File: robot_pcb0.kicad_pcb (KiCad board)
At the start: 2 copper layers, 61.9 x 57.8 mm, 73 parts, among them J1 USB_B_Mini, J10 GPIO, J2 CAN, J3 PWR, J4 Power_terminal, J5 Motor1, J6 Motor2, J7 Motor3, J8 Motor4, J9 UART, P1 SWD, U1 TJA1051TK-3, U2 STM32F40X_LQFP64, U3 BMI160, U4 MCP16311/2, U5 MCP16311/2, U6 DRV8833PW, U7 DRV8833PW, Y1 8M

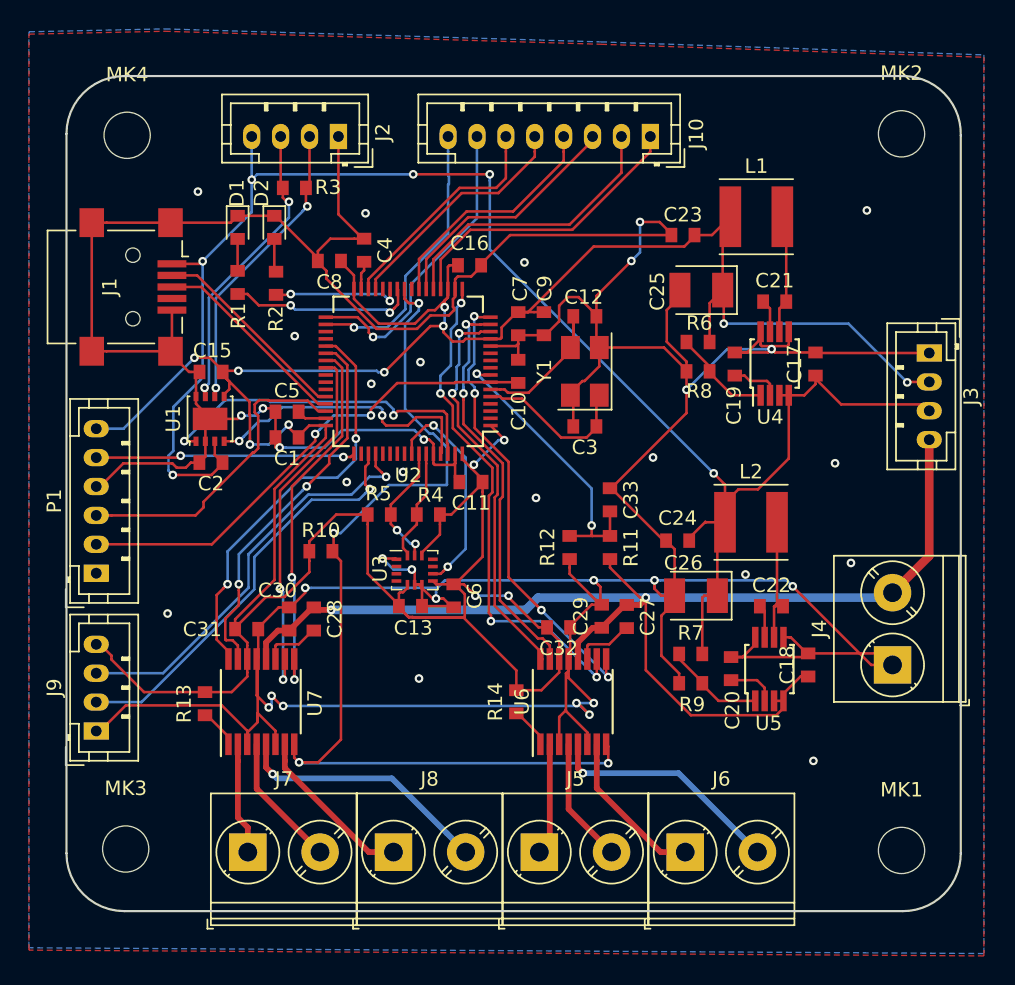
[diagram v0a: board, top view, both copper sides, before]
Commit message: adding an nrf52
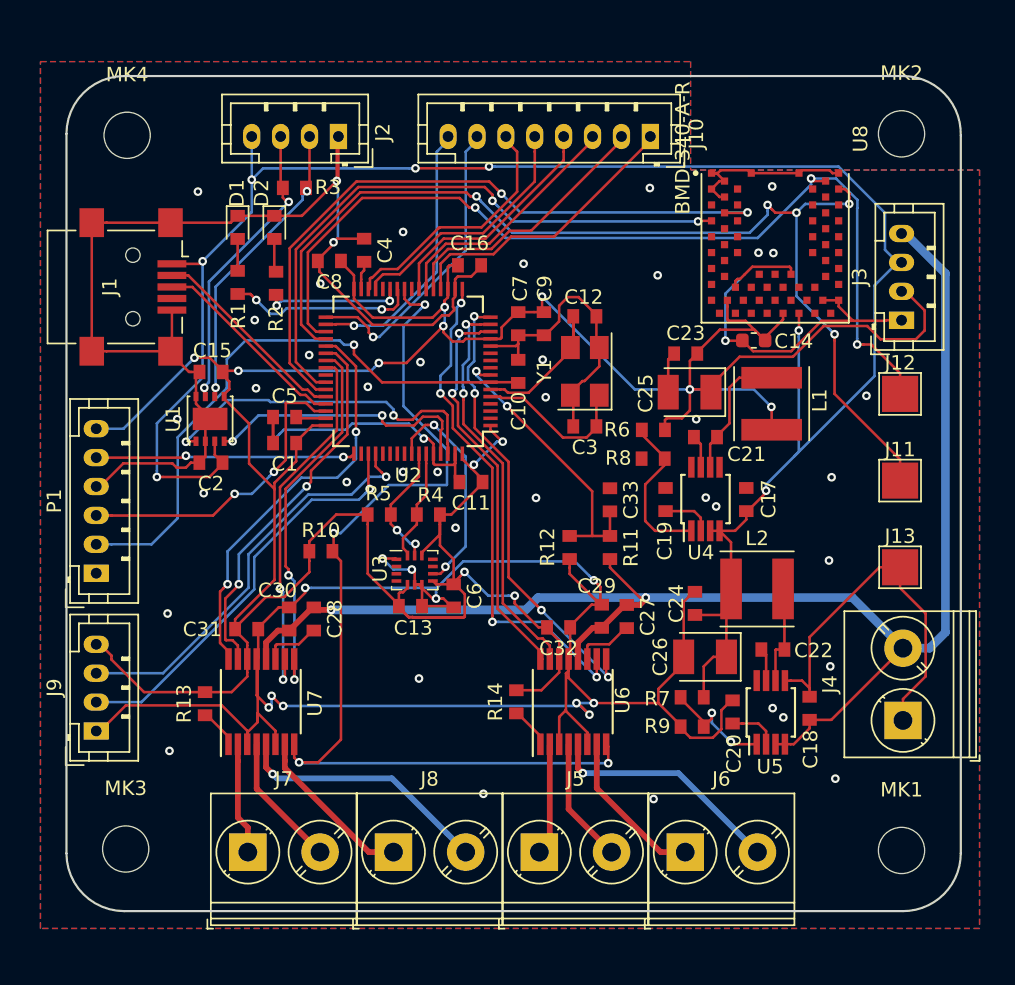
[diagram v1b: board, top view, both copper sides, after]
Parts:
- added C14: 2.2u, Capacitor_SMD:C_0603_1608Metric, F.Cu at (131.9, 89.3)
- added J11: NRFSWDCLK, TestPoint:TestPoint_Pad_2.5x2.5mm, F.Cu at (142.0, 99.0)
- added J12: NRFSWDIO, TestPoint:TestPoint_Pad_2.5x2.5mm, F.Cu at (142.0, 93.0)
- added J13: GND, TestPoint:TestPoint_Pad_2.5x2.5mm, F.Cu at (142.0, 105.0)
- added U8: BMD-340-A-R, crf1:RIGADO_BMD-340-A-R, F.Cu at (133.3, 80.6)
- C31, C32: value 2.2uF -> 2.2u
- moved L1 13.0 mm to (133.1, 93.7), turned to 90 degrees
- moved C19 10.5 mm to (125.8, 100.3)
- moved C17 10.5 mm to (131.4, 100.3)
- moved C21 10.5 mm to (128.5, 96.0)
- moved U4 10.5 mm to (128.5, 100.3)
- moved C23 8.21 mm to (127.2, 90.2)
- moved C25 7.11 mm to (127.4, 92.9)
- moved R6 6.82 mm to (124.9, 95.5)
- moved R8 6.79 mm to (124.9, 97.5)
- moved L2 4.63 mm to (132.1, 106.5)
- moved C24 4.51 mm to (127.8, 107.5), turned to 90 degrees
- moved C26 4.28 mm to (128.5, 111.2)
- moved J4 3.91 mm to (142.2, 115.6)
- moved R7 3.00 mm to (127.6, 114.0)
- moved R9 3.00 mm to (127.6, 116.0)
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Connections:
- U2 pad 35: Net-(U2-Pad35) -> NRFSWDIO
- U2 pad 36: Net-(U2-Pad36) -> NRFSWDCLK
- U2 pad 42: Net-(U2-Pad42) -> NRFRX
- U2 pad 43: Net-(U2-Pad43) -> NRFTX
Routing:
- net NRFSWDCLK: track 0.00 -> 72.8 mm, vias 0 -> 5
- net NRFSWDIO: track 0.00 -> 66.0 mm, vias 0 -> 3
- net NRFTX: track 0.00 -> 47.3 mm, vias 0 -> 2
- net GND: track 375.0 -> 331.2 mm, vias 38 -> 53
- net NRFRX: track 0.00 -> 42.3 mm, vias 0 -> 2
- net 5V: track 118.4 -> 137.6 mm, vias 6 -> 7
- net VCC: track 225.0 -> 231.8 mm, vias 13 -> 12
- net NRST: track 34.4 -> 41.1 mm, vias 2 -> 1
- net Net-(R6-Pad1): track 6.96 -> 11.0 mm
- net Net-(C22-Pad2): track 8.68 -> 6.99 mm
- net GPIO5: track 16.0 -> 17.6 mm
- net GPIO1: track 20.1 -> 18.6 mm
- net Net-(R7-Pad1): track 6.92 -> 8.29 mm, vias 0 -> 2
- net V_IN: track 102.3 -> 103.6 mm
- net Net-(C21-Pad2): track 8.27 -> 9.27 mm
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
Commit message: tweaks
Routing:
- net GND: track 331.2 -> 327.7 mm, vias 53 -> 51
- net VCC: track 231.8 -> 230.8 mm
- net NRFSWDCLK: track 72.8 -> 73.4 mm

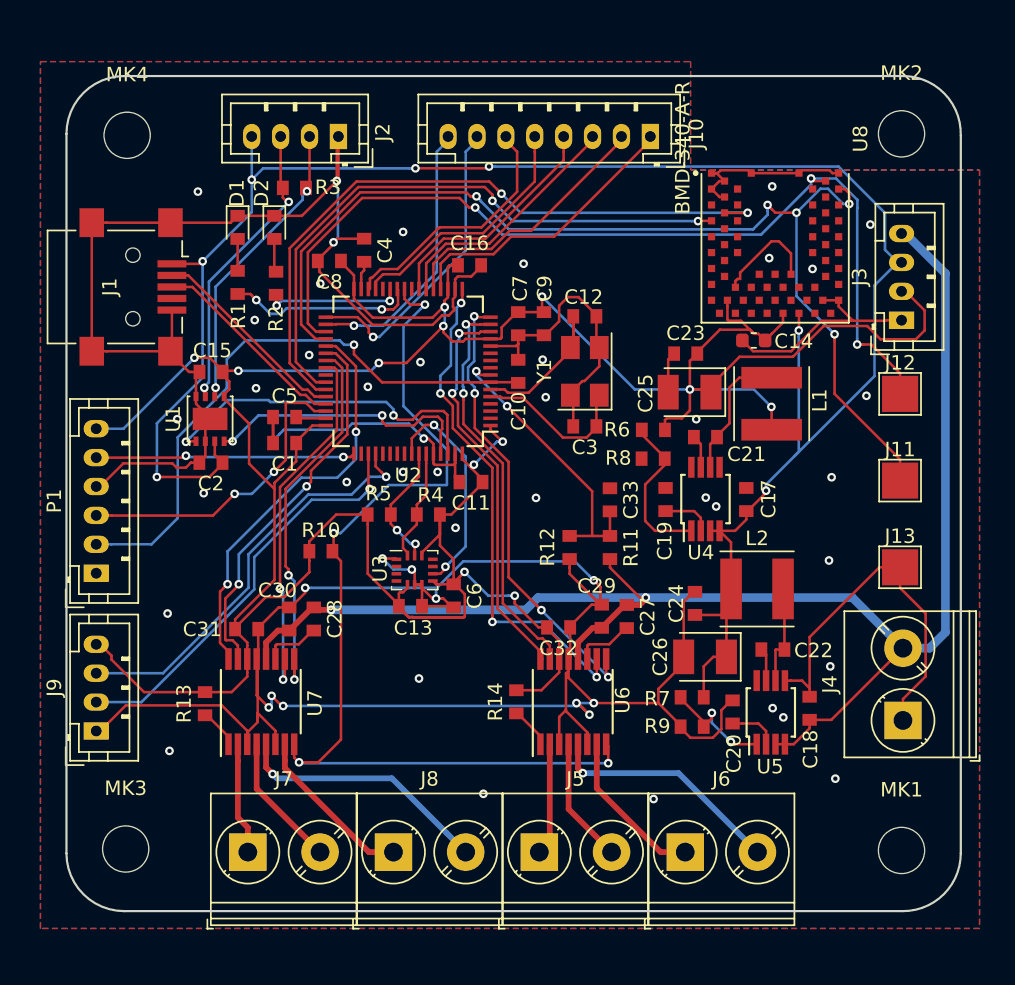
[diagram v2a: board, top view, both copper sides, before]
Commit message: Routing done with nrf52
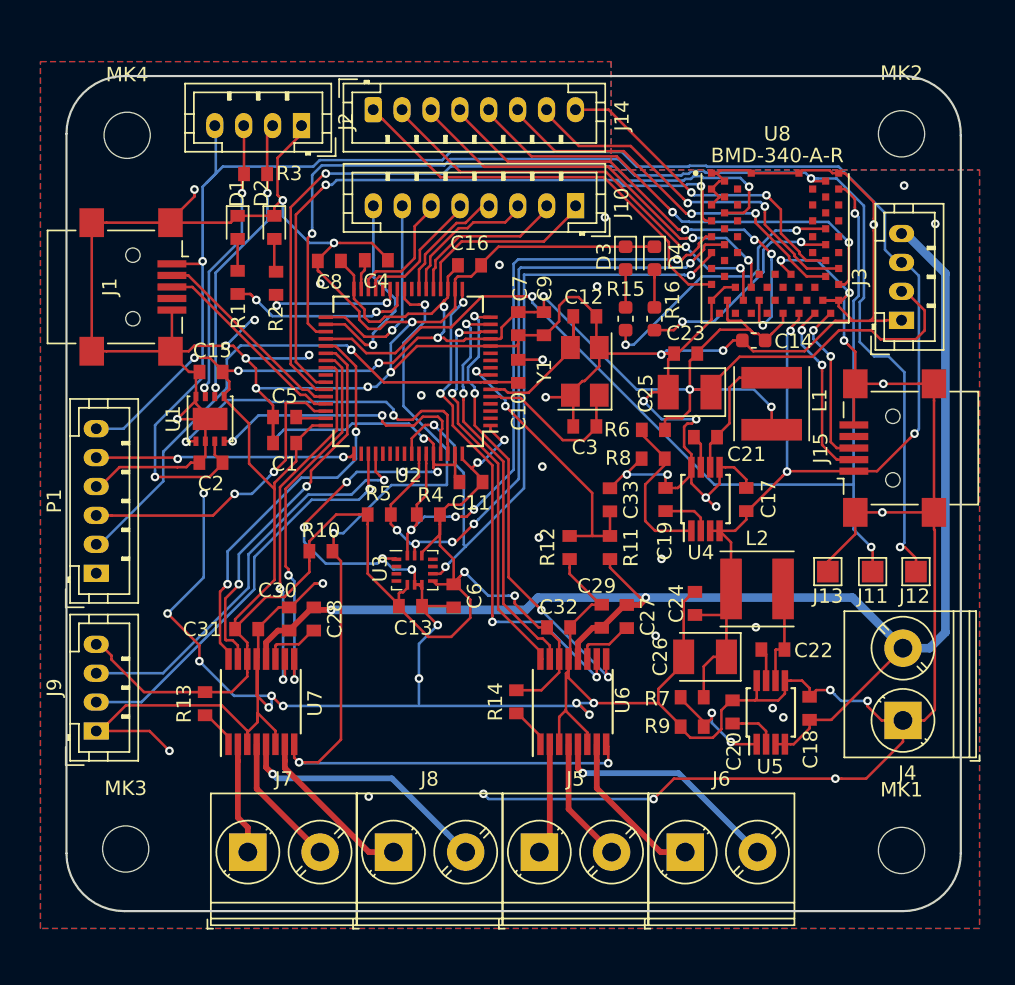
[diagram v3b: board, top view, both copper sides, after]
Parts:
- added D3: RED, LED_SMD:LED_0603_1608Metric, F.Cu at (123.0, 83.6)
- added D4: GREEN, LED_SMD:LED_0603_1608Metric, F.Cu at (125.0, 83.6)
- added J14: NRFGPIO, Connector_JST:JST_PH_B8B-PH-K_1x08_P2.00mm_Vertical, F.Cu at (105.5, 73.3)
- added J15: USB_B_Mini, Connector_USB:USB_Mini-B_Lumberg_2486_01_Horizontal, F.Cu at (141.5, 96.8)
- added R15: 1k, Resistor_SMD:R_0603_1608Metric, F.Cu at (123.0, 87.8)
- added R16: 1k, Resistor_SMD:R_0603_1608Metric, F.Cu at (125.0, 87.8)
- J11, J12, J13: footprint TestPoint:TestPoint_Pad_2.5x2.5mm -> TestPoint:TestPoint_Pad_1.5x1.5mm
- moved J12 12.3 mm to (143.1, 105.3)
- moved J10 7.05 mm to (119.5, 80.0)
- moved J11 6.58 mm to (140.1, 105.3)
- moved J13 5.01 mm to (137.0, 105.3), turned to 180 degrees
- moved R3 2.85 mm to (97.4, 77.8)
- moved J2 2.66 mm to (100.6, 74.4)
- moved C4 1.09 mm to (105.8, 83.8), turned to 180 degrees
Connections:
- U8 pad 10: Net-(U8-Pad10) -> SCL
- U8 pad 11: Net-(U8-Pad11) -> IMU_INT2
- U8 pad 15: Net-(U8-Pad15) -> NRFGPIO1
- U8 pad 19: Net-(U8-Pad19) -> NRFGPIO2
- U8 pad 20: Net-(U8-Pad20) -> NRFGPIO3
- U8 pad 21: Net-(U8-Pad21) -> NRFGPIO4
- U8 pad 31: Net-(U8-Pad31) -> NRFGPIO5
- U8 pad 32: Net-(U8-Pad32) -> NRFGPIO6
- U8 pad 33: Net-(U8-Pad33) -> NRFGPIO7
- U8 pad 34: Net-(U8-Pad34) -> NRFGPIO8
- U8 pad 67: Net-(U8-Pad67) -> NRFUSBD-
- U8 pad 68: Net-(U8-Pad68) -> NRFUSBD+
- U8 pad 9: Net-(U8-Pad9) -> SDA
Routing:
- net GND: track 327.7 -> 551.1 mm, vias 51 -> 68
- net SCL: track 8.78 -> 47.4 mm, vias 2 -> 5
- net SDA: track 7.84 -> 45.3 mm, vias 0 -> 4
- net IMU_INT2: track 15.4 -> 49.6 mm, vias 2 -> 3
- net NRFGPIO4: track 0.00 -> 32.9 mm, vias 0 -> 4
- net NRFGPIO5: track 0.00 -> 32.3 mm, vias 0 -> 2
- net NRFGPIO2: track 0.00 -> 30.4 mm, vias 0 -> 2
- net NRFGPIO1: track 0.00 -> 29.3 mm
- net NRFGPIO3: track 0.00 -> 28.4 mm, vias 0 -> 2
- net NRFGPIO6: track 0.00 -> 26.8 mm, vias 0 -> 2
- net NRFGPIO7: track 0.00 -> 25.8 mm, vias 0 -> 2
- net NRFGPIO8: track 0.00 -> 22.7 mm, vias 0 -> 2
- net Net-(R15-Pad1): track 0.00 -> 19.1 mm, vias 0 -> 2
- net NRFSWDIO: track 65.8 -> 81.3 mm
- net Net-(R16-Pad1): track 0.00 -> 15.4 mm, vias 0 -> 2
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
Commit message: added a pic and some tweaks
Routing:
- net NRFGPIO8: track 22.7 -> 23.2 mm
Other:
- rule pad_to_mask_clearance: 0.2 -> 0.02
- board text added: "Benjamin Vedder & Joel Svensson FMRC v1.0"
